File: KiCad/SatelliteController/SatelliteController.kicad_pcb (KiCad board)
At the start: 2 copper layers, 150 x 100 mm, 191 parts, among them J1 CONN_ICSP, J10 CONN_UMBILICAL, J11 CONN_SORENOID_VALVE, J12 RELAY_POWER, J15 CONN_RS485, J2 CONN_USB, J3 USB_B_Micro, J4 DC_IN, J5 TO_CONVERTER, J6 FROM_CONVERTER, J7 CONN_STATUS_PANEL, J8 CONN_PANEL_BAORD_2, J9 CONN_N2O_PRESS, Q1 TJ8S06M3L, Q10 AO3400A, Q11 AO3400A, Q12 AO3400A, Q2 TJ8S06M3L, Q3 2SC3325-Y, Q4 AO3400A, Q5 AO3400A, Q6 AO3400A, Q7 AO3400A, Q8 AO3400A, Q9 AO3400A, SW1 SW_Push, SW11 SW_Push, SW17 SW_Push, SW18 SW_Push, SW19 SW_Push, SW2 SW_Push, SW20 SW_Push, SW21 SW_Push, SW22 SW_Push, SW23 SW_Push, SW24 SW_Push, SW25 SW_Push, U1 FT232RL, U2 ATMEGA2560-16AUR, U3 NJM7805SDL1, U4 INA219BIDCNT, U5 INA219BIDCNT, U6 TLP785F, U7 TLP785F, U8 LTC485CN8#PBF, U9 MCP3208, Y1 HUSG-16.000-20

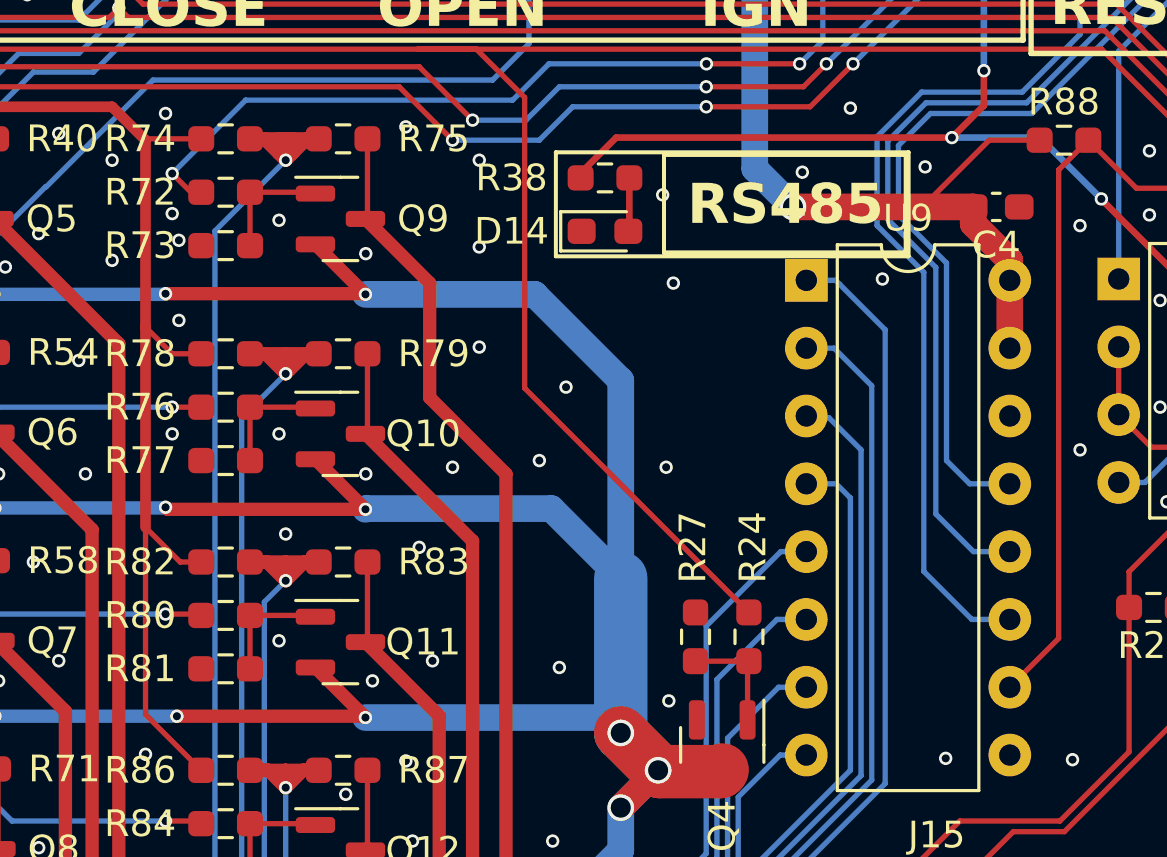
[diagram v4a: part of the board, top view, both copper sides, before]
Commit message: DRCを解決
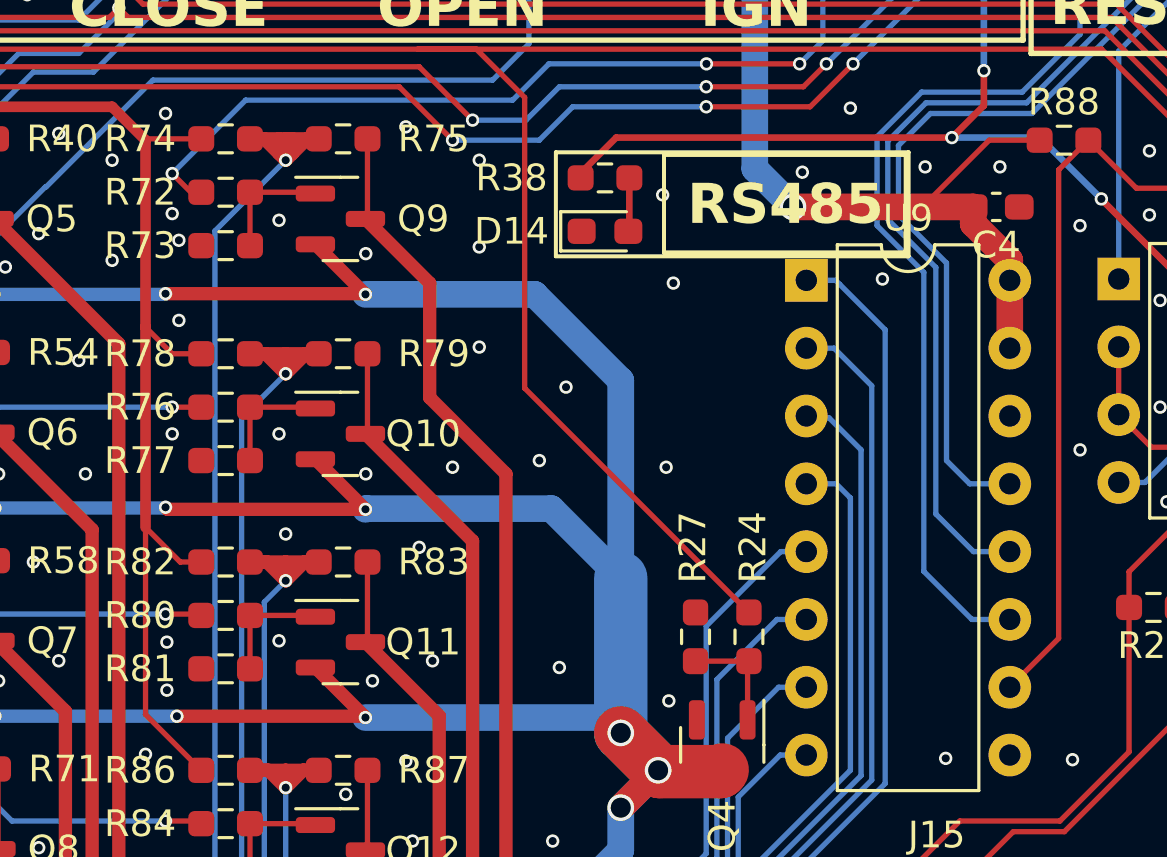
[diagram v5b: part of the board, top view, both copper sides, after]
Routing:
- net GND: vias 313 -> 316
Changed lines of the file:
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@@
         (effects (font (size 1 1) (thickness 0.15)))
     )
+    (fp_text user "Backward" (at 2 0 90 unlocked) (layer "F.Fab")
+        (effects (font (size 1 1) (thickness 0.15)) (justify bottom))
+    )
     (fp_text user "Forward" (at 2 3.5 90 unlocked) (layer "F.Fab")
         (effects (font (size 1 1) (thickness 0.15)) (justify bottom))
@@
         (effects (font (size 1 1) (thickness 0.15)))
     )
-    (fp_text user "Backward" (at 2 0 90 unlocked) (layer "F.Fab")
-        (effects (font (size 1 1) (thickness 0.15)) (justify bottom))
-    )
     (fp_rect (start -5.22 9.3) (end 8.42 -4.24)
       (stroke (width 0.12) (type default)) (fill none) (layer "F.SilkS"))
@@
   (via (at 172.133174 80.888716) (size 0.5) (drill 0.3) (layers "F.Cu" "B.Cu") (free) (net 1))
   (via (at 55.85 59.55) (size 0.5) (drill 0.3) (layers "F.Cu" "B.Cu") (free) (net 1))
+  (via (at 99.630705 84.846793) (size 0.5) (drill 0.3) (layers "F.Cu" "B.Cu") (free) (net 1))
   (via (at 121.35 68.8) (size 0.5) (drill 0.3) (layers "F.Cu" "B.Cu") (free) (net 1))
   (via (at 166.133174 70.388716) (size 0.5) (drill 0.3) (layers "F.Cu" "B.Cu") (free) (net 1))
@@
   (via (at 171.75 123) (size 0.5) (drill 0.3) (layers "F.Cu" "B.Cu") (free) (net 1))
   (via (at 131.830705 69.446793) (size 0.5) (drill 0.3) (layers "F.Cu" "B.Cu") (free) (net 1))
+  (via (at 68.430705 104.446793) (size 0.5) (drill 0.3) (layers "F.Cu" "B.Cu") (free) (net 1))
   (via (at 64.380705 103.346793) (size 0.5) (drill 0.3) (layers "F.Cu" "B.Cu") (free) (net 1))
   (via (at 126.633174 77.888716) (size 0.5) (drill 0.3) (layers "F.Cu" "B.Cu") (free) (net 1))
@@
   (via (at 116.380705 94.096793) (size 0.5) (drill 0.3) (layers "F.Cu" "B.Cu") (free) (net 1))
   (via (at 166.383174 82.888716) (size 0.5) (drill 0.3) (layers "F.Cu" "B.Cu") (free) (net 1))
+  (via (at 68.430705 102.646793) (size 0.5) (drill 0.3) (layers "F.Cu" "B.Cu") (free) (net 1))
   (via (at 184.380705 59.596793) (size 0.5) (drill 0.3) (layers "F.Cu" "B.Cu") (free) (net 1))
   (via (at 172.133174 102.138716) (size 0.5) (drill 0.3) (layers "F.Cu" "B.Cu") (free) (net 1))
